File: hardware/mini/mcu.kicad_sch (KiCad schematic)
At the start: 20 parts, among them J1 USB_C_Receptacle_USB2.0_16P, U2 AP63203WU, U3 STM32F103C8Tx, Y1 16MHz

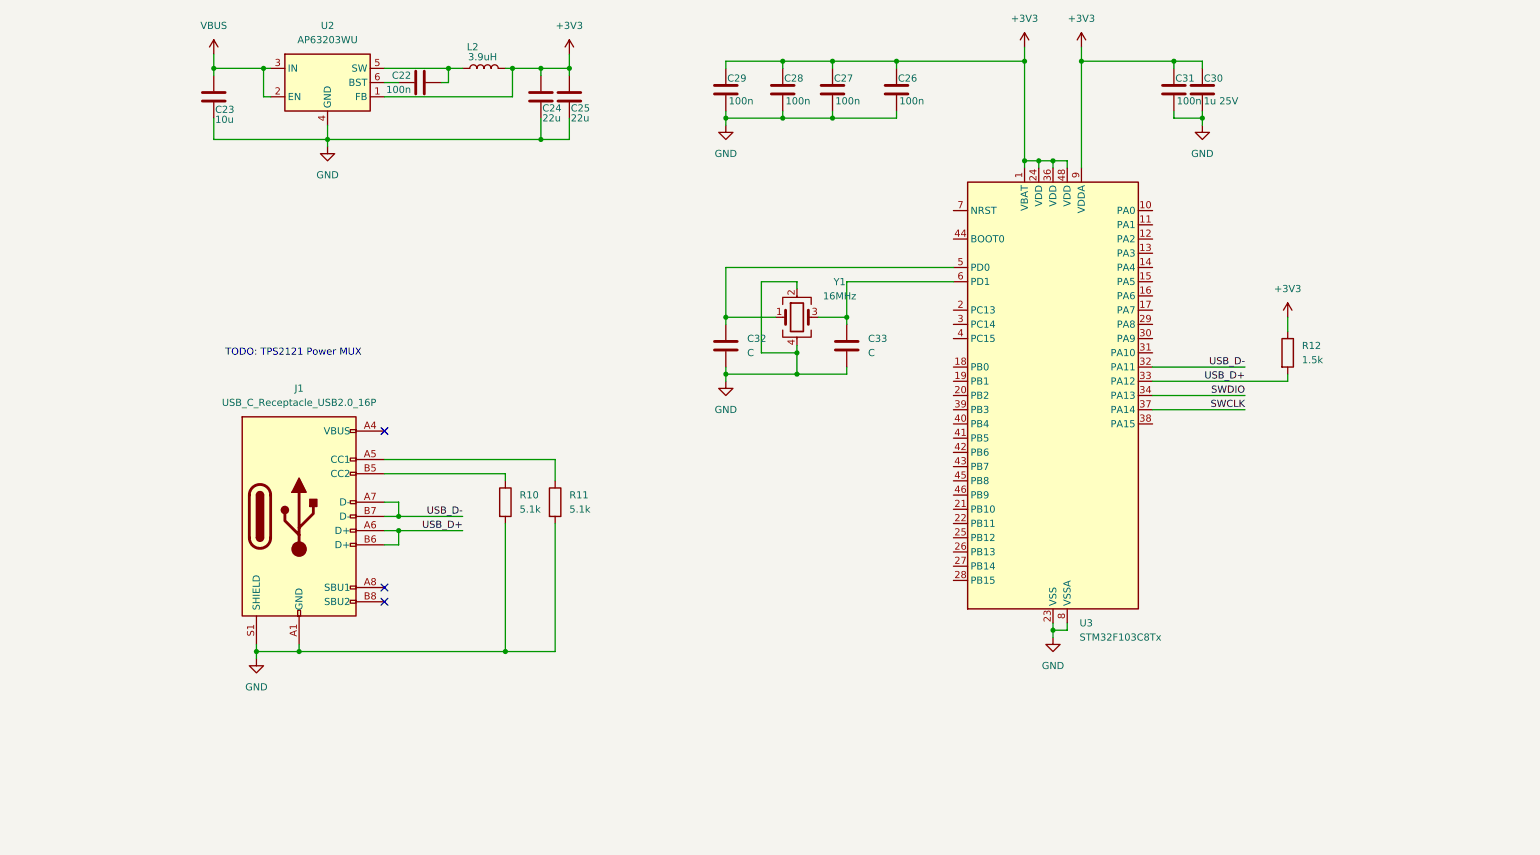
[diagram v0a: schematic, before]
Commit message: add interface & RP2040
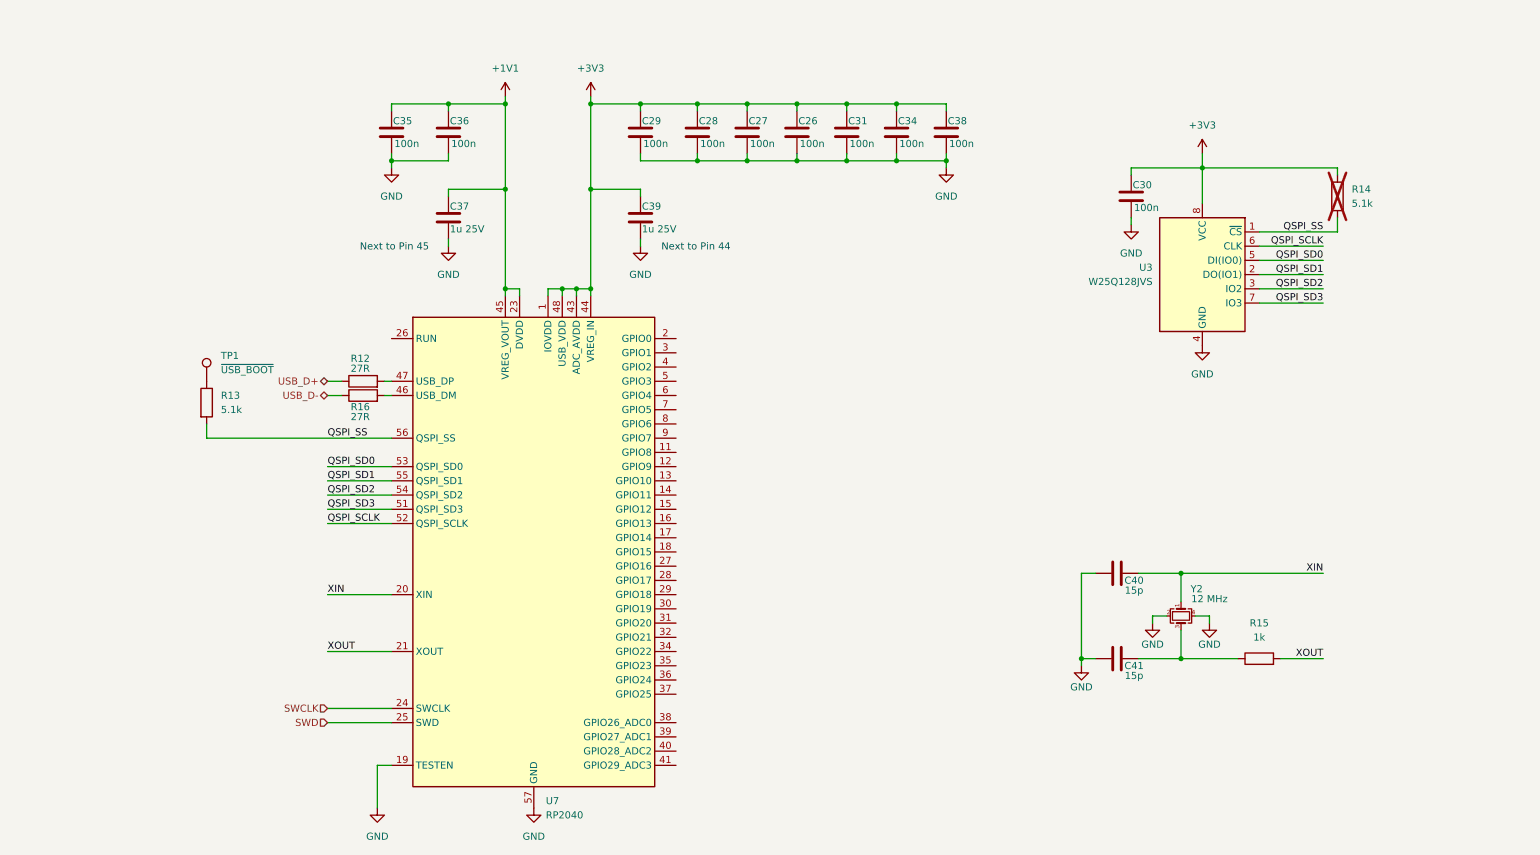
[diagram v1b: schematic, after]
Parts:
- removed C22: 100n, Capacitor_SMD:C_0402_1005Metric, symbol Device:C
- removed C23: 10u, Capacitor_SMD:C_1206_3216Metric, symbol Device:C
- removed C24, C25: 22u, Capacitor_SMD:C_0603_1608Metric, symbol Device:C
- removed C32, C33: C, symbol Device:C
- removed J1: USB_C_Receptacle_USB2.0_16P, symbol Connector:USB_C_Receptacle_USB2.0_16P
- removed L2: 3.9uH, Inductor_SMD:L_Changjiang_FNR5020S, symbol Device:L
- removed R10, R11: 5.1k, symbol Device:R
- removed U2: AP63203WU, Package_TO_SOT_SMD:TSOT-23-6, symbol Regulator_Switching:AP63203WU
- removed U3: STM32F103C8Tx, Package_QFP:LQFP-48_7x7mm_P0.5mm, symbol MCU_ST_STM32F1:STM32F103C8Tx
- removed Y1: 16MHz, symbol Device:Crystal_GND24
- added C34, C35, C36, C38: 100n, Capacitor_SMD:C_0402_1005Metric, symbol Device:C
- added C37, C39: 1u 25V, Capacitor_SMD:C_0402_1005Metric, symbol Device:C
- added C40, C41: 15p, symbol Device:C
- added R13, R14: 5.1k, symbol Device:R
- added R15: 1k, symbol Device:R
- added R16: 27R, symbol Device:R
- added TP1: ~{USB_BOOT}, symbol Connector:TestPoint
- added U3: W25Q128JVS, Package_SO:SOIC-8_5.23x5.23mm_P1.27mm, symbol Memory_Flash:W25Q128JVS
- added U7: RP2040, Package_DFN_QFN:QFN-56-1EP_7x7mm_P0.4mm_EP3.2x3.2mm, symbol MCU_RaspberryPi:RP2040
- added Y2: 12 MHz, symbol Device:Crystal_GND24_Small
- C30: value 1u 25V -> 100n; LCSC C52923 -> C307331
- R12: value 1.5k -> 27R; LCSC C25867 -> (none)
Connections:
- net +3V3: now also C34.1, C38.1, C39.1, R14.1, U3.8 (VCC), U7.1 (IOVDD), U7.10 (IOVDD), U7.22 (IOVDD), U7.33 (IOVDD), U7.42 (IOVDD), U7.43 (ADC_AVDD), U7.44 (VREG_IN), U7.48 (USB_VDD), U7.49 (IOVDD); no longer R12.1
- net GND: now also C34.2, C35.2, C36.2, C37.2, C38.2, C39.2, C40.1, C41.1, U3.4 (GND), U7.19 (TESTEN), U7.57 (GND), Y2.2, Y2.4
- net SWCLK: now also U7.24 (SWCLK)
- net USB_D+: now also R12.1; no longer R12.2
- net USB_D-: now also R16.1
- new net: R12.2, U7.47 (USB_DP)
- new net: C41.2, R15.1, Y2.3
- new net: R16.2, U7.46 (USB_DM)
- new net: R13.1, TP1.1
- new net +1V1: C35.1, C36.1, C37.1, U7.23 (DVDD), U7.45 (VREG_VOUT), U7.50 (DVDD)
- new net QSPI_SCLK: U3.6 (CLK), U7.52 (QSPI_SCLK)
- new net QSPI_SD0: U3.5 (DI(IO0)), U7.53 (QSPI_SD0)
- new net QSPI_SD1: U3.2 (DO(IO1)), U7.55 (QSPI_SD1)
- new net QSPI_SD2: U3.3 (IO2), U7.54 (QSPI_SD2)
- new net QSPI_SD3: U3.7 (IO3), U7.51 (QSPI_SD3)
- new net QSPI_SS: R13.2, R14.2, U3.1 (~{CS}), U7.56 (QSPI_SS)
- new net SWD: U7.25 (SWD)
- new net XIN: C40.2, U7.20 (XIN), Y2.1
- new net XOUT: R15.2, U7.21 (XOUT)
- no-connect marks 3 -> 0
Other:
- note added: "Next to Pin 44"
- note added: "Next to Pin 45"
- note removed: "TODO: TPS2121 Power MUX"
- moved on the sheet: C26, C27, C28, C29, C31

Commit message: finalize parts in schematic
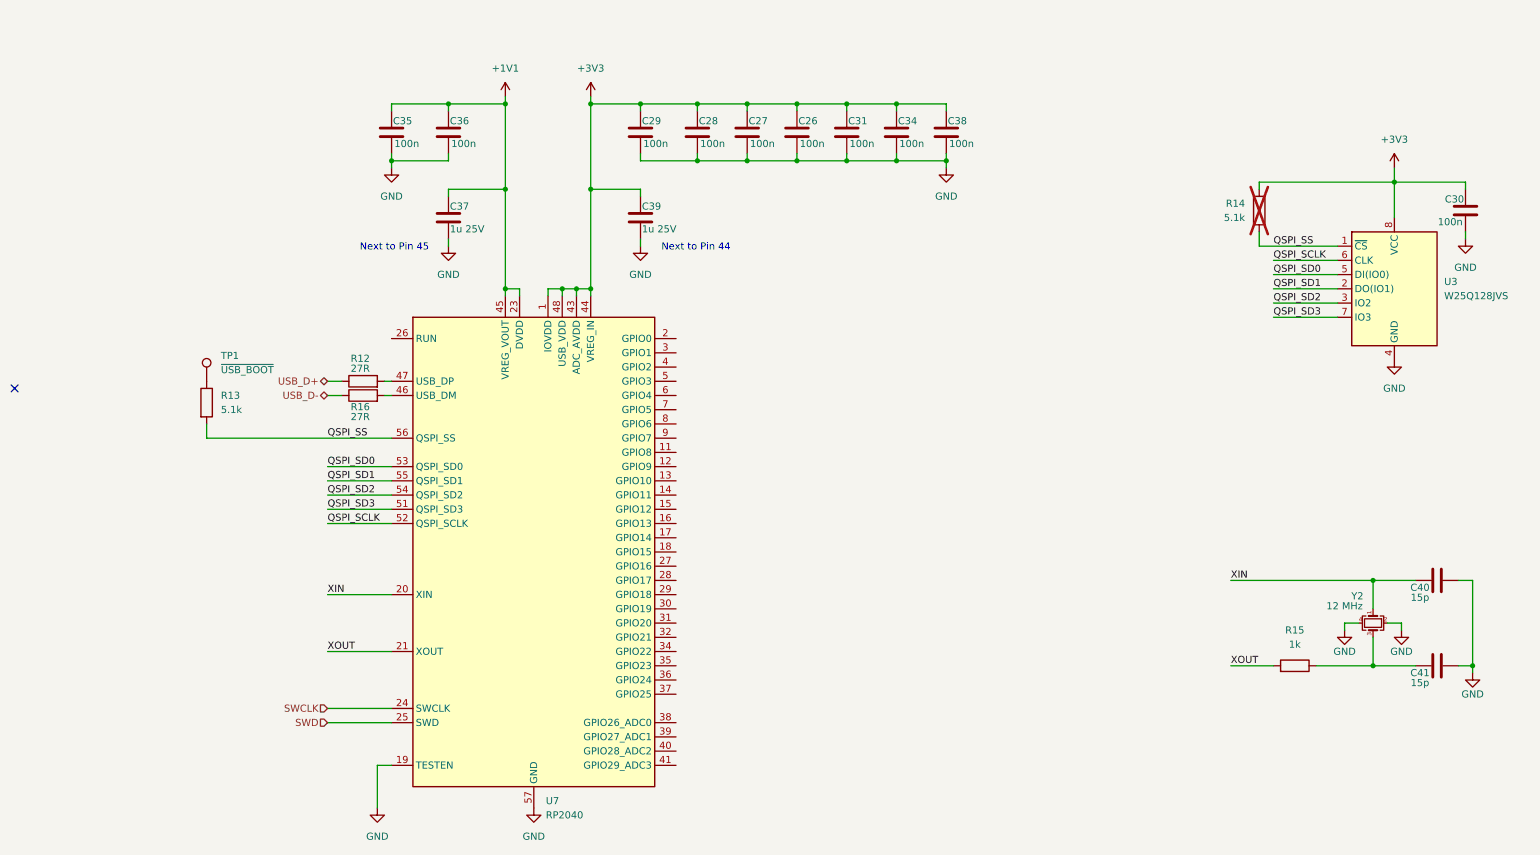
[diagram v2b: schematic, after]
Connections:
- no-connect marks 0 -> 1
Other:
- moved on the sheet: C30, C40, C41, R14, R15, U3, Y2

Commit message: route most
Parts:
- renumbered C29 to C38, C28 to C40, C27 to C41, C26 to C42, C31 to C43, C34 to C44, C38 to C45, C40 to C46, C41 to C47, C30 to C48, R13 to R17, R12 to R18, R16 to R19, R14 to R20, R15 to R21, U7 to U6, U3 to U7, Y2 to Y1
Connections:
- net ROW_3: now reaches U6.11 (GPIO8)
- net ROW_4: now reaches U6.12 (GPIO9)
- net SENS_INT_A: now reaches U6.15 (GPIO12)
- net SENS_INT_B: now reaches U6.16 (GPIO13)
- net DISP_BACKLIGHT: now reaches U6.18 (GPIO15)
- net I2C0_SDA: now reaches U6.2 (GPIO0)
- net SPI0_RX: now reaches U6.27 (GPIO16)
- net SPI0_CS: now reaches U6.28 (GPIO17)
- net SPI0_SCK: now reaches U6.29 (GPIO18)
- net I2C0_SCL: now reaches U6.3 (GPIO1)
- net SPI0_TX: now reaches U6.30 (GPIO19)
- net DISP_RST: now reaches U6.31 (GPIO20)
- net DISP_RS: now reaches U6.32 (GPIO21)
- net I2C1_SDA: now reaches U6.34 (GPIO22)
- net I2C1_SCL: now reaches U6.35 (GPIO23)
- net EN_B: now reaches U6.36 (GPIO24)
- net EN_A: now reaches U6.37 (GPIO25)
- net TEMP_B: now reaches U6.38 (GPIO26_ADC0)
- net TEMP_A: now reaches U6.39 (GPIO27_ADC1)
- net USB_INT: now reaches U6.4 (GPIO2)
- net COL_0: now reaches U6.5 (GPIO3)
- net COL_1: now reaches U6.6 (GPIO4)
- net ROW_0: now reaches U6.7 (GPIO5)
- net ROW_1: now reaches U6.8 (GPIO6)
- net ROW_2: now reaches U6.9 (GPIO7)
- no-connect marks 1 -> 2
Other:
- note added: "BUTTON MATRIX"
- note added: "INA226 x2"
- note added: "NTC TEMP"
- note added: "SPI TFT Display ST7789T3"
- note added: "STUSB4500 TPS55289 x2"
- note added: "TPS55289 ENABLE"

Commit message: ERC run
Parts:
- added R15: 0R, symbol Device:R
- added R18, R19, R20, R21, R22, R23, R24: 5.1k, symbol Device:R
- added TP3: P14, symbol Connector:TestPoint
- added TP4: P16, symbol Connector:TestPoint
- added TP5: P28, symbol Connector:TestPoint
- added TP6: P29, symbol Connector:TestPoint
- R25: renamed from R20; now fitted
- renumbered C35 to C30, C36 to C31, C37 to C32, C38 to C33, C39 to C34, C40 to C35, C41 to C36, C42 to C37, C43 to C38, C44 to C39, C45 to C40, C46 to C41, C47 to C42, C48 to C43, R17 to R14, R18 to R16, R19 to R17, R21 to R26, U6 to U5, U7 to U6
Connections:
- net +3V3: now also R15.1, R18.1, R19.1, R20.1, R21.1, R22.1, R23.1, R24.1
- net COL_0: now also U5.6 (GPIO4); no longer U5.5 (GPIO3)
- net COL_1: now also U5.7 (GPIO5); no longer U5.6 (GPIO4)
- net I2C0_SCL: now also R19.2
- net I2C0_SDA: now also R18.2
- net I2C1_SCL: now also R24.2
- net I2C1_SDA: now also R21.2
- net ROW_0: now also U5.8 (GPIO6); no longer U5.7 (GPIO5)
- net ROW_1: now also U5.9 (GPIO7); no longer U5.8 (GPIO6)
- net ROW_2: now also U5.11 (GPIO8); no longer U5.9 (GPIO7)
- net ROW_3: now also U5.12 (GPIO9); no longer U5.11 (GPIO8)
- net ROW_4: now also U5.13 (GPIO10); no longer U5.12 (GPIO9)
- net SENS_INT_A: now also R20.2
- net SENS_INT_B: now also R23.2
- net USB_INT: now also R22.2
- net LED_DATA: now reaches U5.14 (GPIO11)
- net P14: now reaches U5.17 (GPIO14)
- net P14: now also TP3.1
- net at U5.26 (RUN): now also R15.2
- net P28: now reaches U5.40 (GPIO28_ADC2)
- net P28: now also TP5.1
- net P29: now reaches U5.41 (GPIO29_ADC3)
- net P29: now also TP6.1
- net SPI0_RX renamed P16
- net P16: now also TP4.1
- new net USB_RST: U5.5 (GPIO3)
- no-connect marks 2 -> 0
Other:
- note added: "ST7789T3"
- note removed: "SPI TFT Display ST7789T3"
- moved on the sheet: C41, C42, R26, Y1

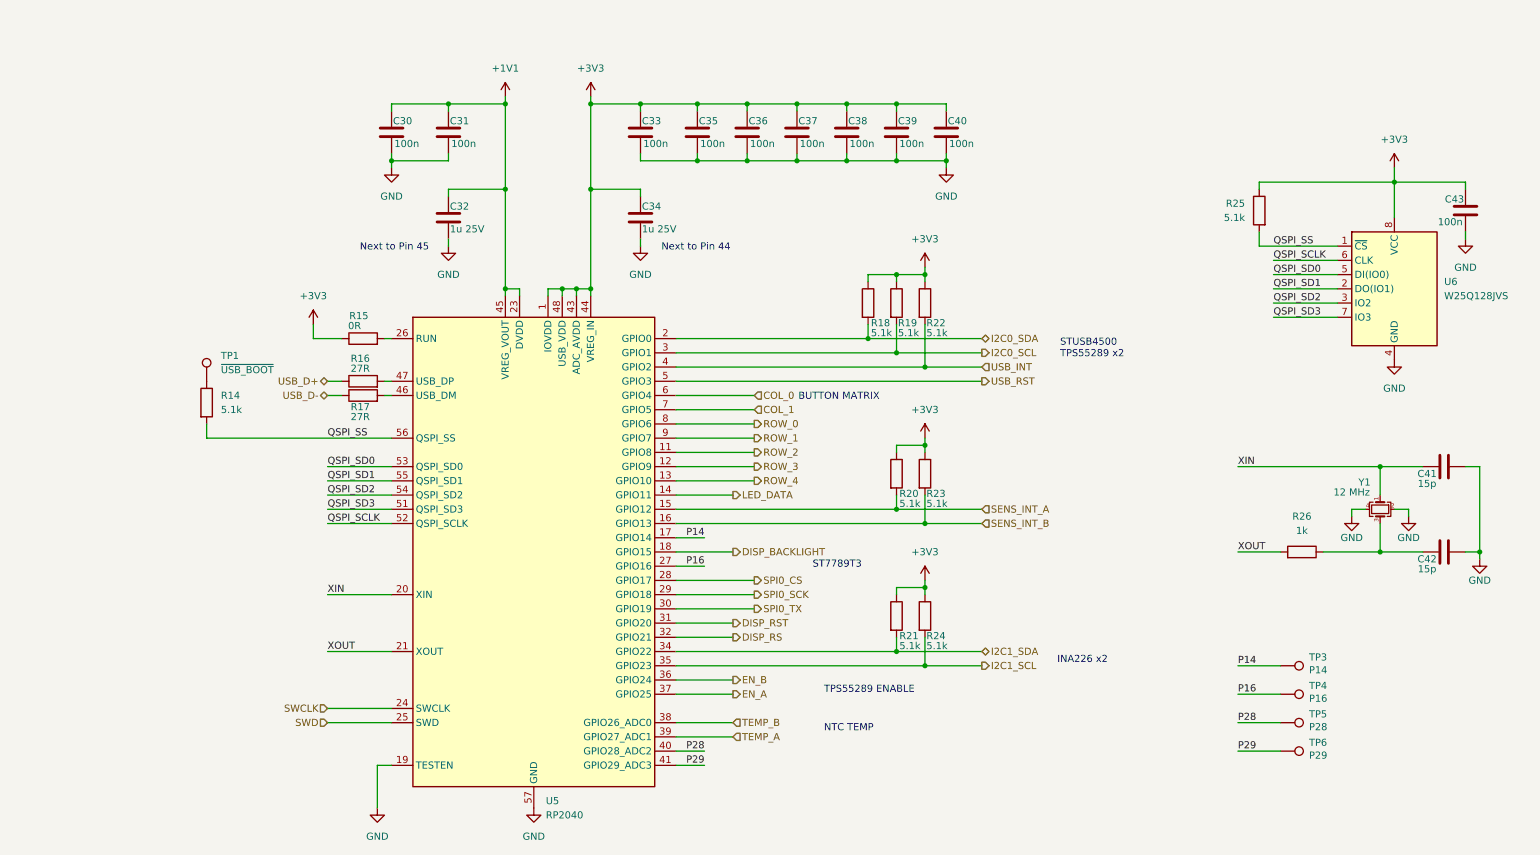
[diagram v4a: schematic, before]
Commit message: assign footprints & LCSC id
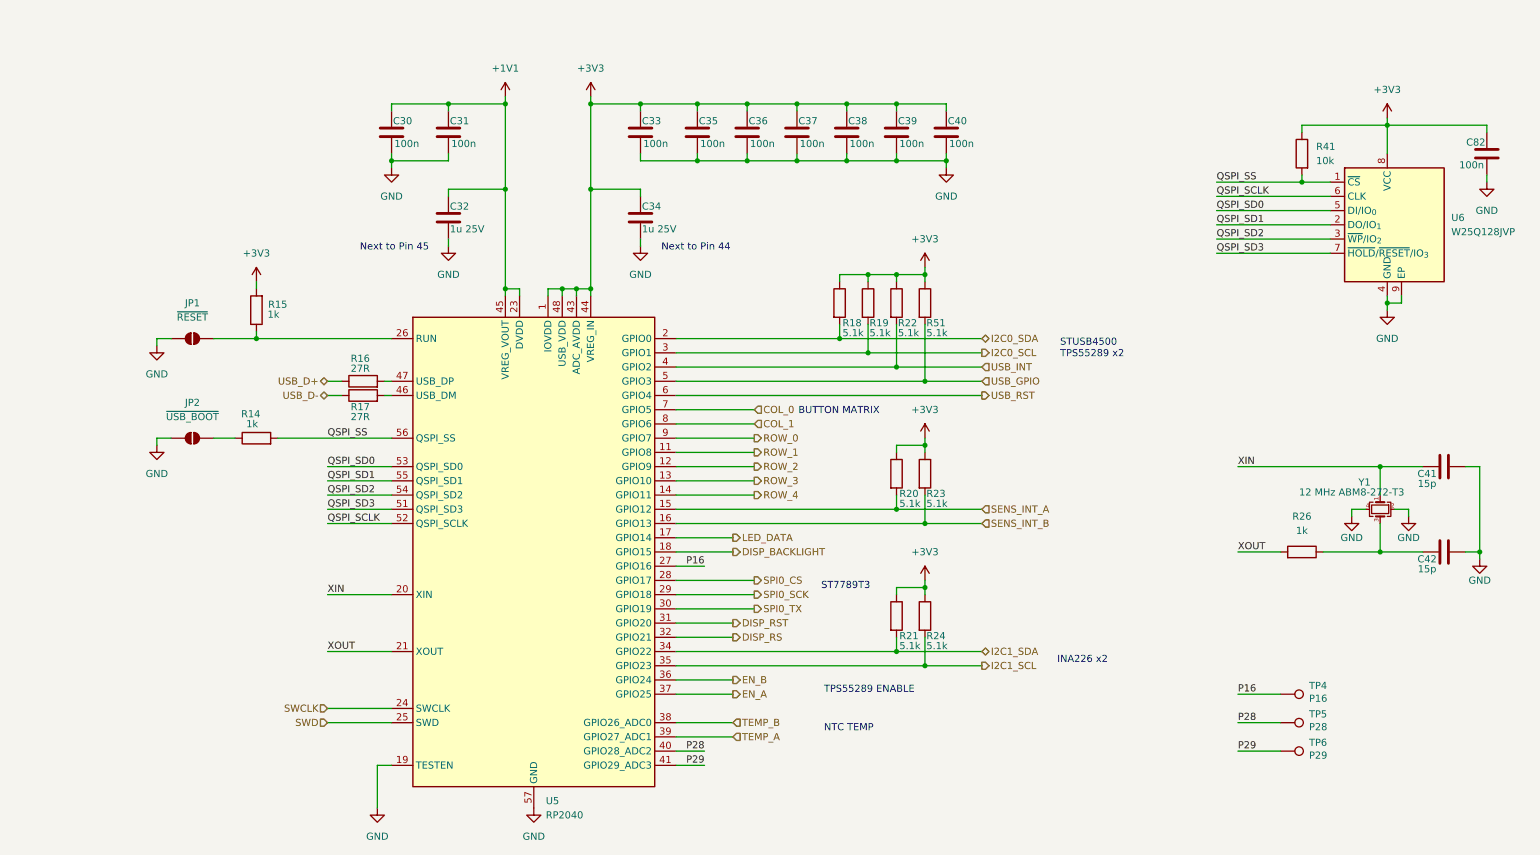
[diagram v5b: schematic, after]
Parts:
- removed C43: 100n, Capacitor_SMD:C_0402_1005Metric, symbol Device:C
- removed R25: 5.1k, symbol Device:R
- removed TP1: ~{USB_BOOT}, symbol Connector:TestPoint
- removed TP3: P14, symbol Connector:TestPoint
- removed U6: W25Q128JVS, Package_SO:SOIC-8_5.23x5.23mm_P1.27mm, symbol Memory_Flash:W25Q128JVS
- added C82: 100n, Capacitor_SMD:C_0402_1005Metric, symbol Device:C
- added JP1: ~{RESET}, symbol Jumper:SolderJumper_2_Open
- added JP2: ~{USB_BOOT}, symbol Jumper:SolderJumper_2_Open
- added R41: 10k, Resistor_SMD:R_0402_1005Metric, symbol Device:R
- added R51: 5.1k, Resistor_SMD:R_0402_1005Metric, symbol Device:R
- added U6: W25Q128JVP, Package_SON:WSON-8-1EP_6x5mm_P1.27mm_EP3.4x4.3mm, symbol Memory_Flash:W25Q128JVP
- C41, C42: footprint (none) -> Capacitor_SMD:C_0402_1005Metric; LCSC (none) -> C1548
- R14: value 5.1k -> 1k; footprint (none) -> Resistor_SMD:R_0402_1005Metric; LCSC C25905 -> C11702
- R15: value 0R -> 1k; footprint (none) -> Resistor_SMD:R_0402_1005Metric; LCSC (none) -> C11702
- R16, R17: footprint (none) -> Resistor_SMD:R_0402_1005Metric; LCSC (none) -> C138021
- R18, R19, R20, R21, R22, R23, R24: footprint (none) -> Resistor_SMD:R_0402_1005Metric
- R26: footprint (none) -> Resistor_SMD:R_0402_1005Metric; LCSC (none) -> C11702
- TP4, TP5, TP6: footprint (none) -> TestPoint:TestPoint_Pad_D1.0mm
- U5: LCSC (none) -> C2040
- Y1: value 12 MHz -> 12 MHz ABM8-272-T3; footprint (none) -> Crystal:Crystal_SMD_Abracon_ABM8AIG-4Pin_3.2x2.5mm; LCSC (none) -> C20625731
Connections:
- net P14 is gone; now on net LED_DATA: U5.17 (GPIO14)
- net +3V3: now also R15.2, C82.1, R41.1, R51.1, U6.8 (VCC); no longer R15.1
- net COL_0: now also U5.7 (GPIO5); no longer U5.6 (GPIO4)
- net COL_1: now also U5.8 (GPIO6); no longer U5.7 (GPIO5)
- net GND: now also C82.2, JP1.1 (A), JP2.1 (A), U6.4 (GND), U6.9 (EP)
- net LED_DATA: no longer U5.14 (GPIO11)
- net QSPI_SCLK: now also U6.6 (CLK)
- net QSPI_SD0: now also U6.5 (DI/IO_{0})
- net QSPI_SD1: now also U6.2 (DO/IO_{1})
- net QSPI_SD2: now also U6.3 (~{WP}/IO_{2})
- net QSPI_SD3: now also U6.7 (~{HOLD}/~{RESET}/IO_{3})
- net QSPI_SS: now also R41.2, U6.1 (~{CS})
- net ROW_0: now also U5.9 (GPIO7); no longer U5.8 (GPIO6)
- net ROW_1: now also U5.11 (GPIO8); no longer U5.9 (GPIO7)
- net ROW_2: now also U5.12 (GPIO9); no longer U5.11 (GPIO8)
- net ROW_3: now also U5.13 (GPIO10); no longer U5.12 (GPIO9)
- net ROW_4: now also U5.14 (GPIO11); no longer U5.13 (GPIO10)
- net USB_RST: now also U5.6 (GPIO4); no longer U5.5 (GPIO3)
- net at U5.26 (RUN): now also R15.1, JP1.2 (B); no longer R15.2
- net at R14.1: now also JP2.2 (B)
- new net USB_GPIO: R51.2, U5.5 (GPIO3)
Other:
- moved on the sheet: R14, R18, R19, R22

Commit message: import to PCB
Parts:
- JP1, JP2: footprint (none) -> Jumper:SolderJumper-2_P1.3mm_Open_RoundedPad1.0x1.5mm
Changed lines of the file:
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@@
 			)
 		)
-		(property "Footprint" ""
+		(property "Footprint" "Jumper:SolderJumper-2_P1.3mm_Open_RoundedPad1.0x1.5mm"
 			(at 31.75 102.87 0)
 			(effects
@@
 			)
 		)
-		(property "Footprint" ""
+		(property "Footprint" "Jumper:SolderJumper-2_P1.3mm_Open_RoundedPad1.0x1.5mm"
 			(at 31.75 85.09 0)
 			(effects
